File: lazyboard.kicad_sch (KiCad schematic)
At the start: 15 parts, among them J1 QWIIC/STEMMA, J2 Conn_01x06_Pin, J3 Conn_01x06_Pin, J4 Conn_01x03_Pin, J5 Conn_01x06_Pin, J6 Conn_01x06_Pin, P1 USB_C_Plug_USB2.0, SW1 SW_Push, SW2 SW_Push, U2 AP2112K-3.3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

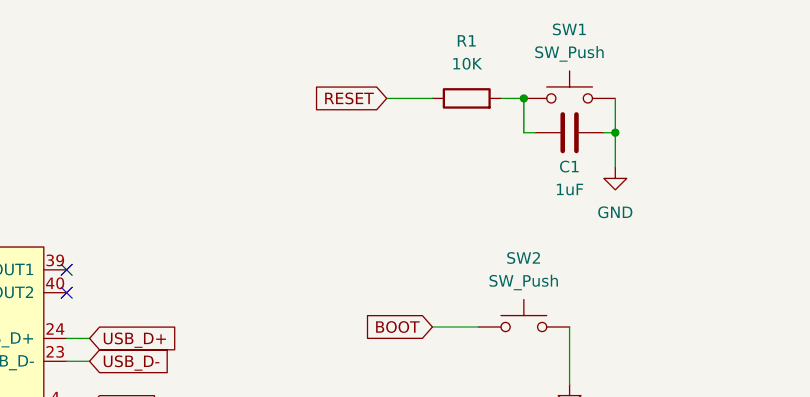
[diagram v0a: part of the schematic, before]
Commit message: fixed reset bug
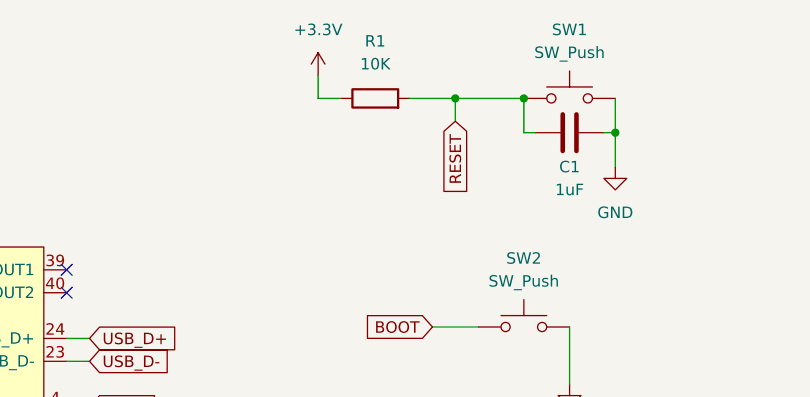
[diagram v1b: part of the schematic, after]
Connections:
- net +3.3V: now also R1.1
- net RESET: now also C1.1, R1.2, SW1.1; no longer R1.1
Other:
- moved on the sheet: R1
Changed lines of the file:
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@@
   (junction (at 85.09 124.46) (diameter 0) (color 0 0 0 0)
+  )
+  (junction (at 173.99 26.67) (diameter 0) (color 0 0 0 0)
   )
   (junction (at 53.34 156.21) (diameter 0) (color 0 0 0 0)
@@
     (stroke (width 0) (type default))
   )
-  (wire (pts (xy 179.07 26.67) (xy 181.61 26.67))
+  (wire (pts (xy 168.91 26.67) (xy 173.99 26.67))
     (stroke (width 0) (type default))
   )
@@
     (stroke (width 0) (type default))
   )
+  (wire (pts (xy 158.75 26.67) (xy 161.29 26.67))
+    (stroke (width 0) (type default))
+  )
   (wire (pts (xy 130.81 73.66) (xy 133.35 73.66))
     (stroke (width 0) (type default))
@@
     (stroke (width 0) (type default))
   )
-  (wire (pts (xy 166.37 26.67) (xy 171.45 26.67))
+  (wire (pts (xy 173.99 26.67) (xy 181.61 26.67))
     (stroke (width 0) (type default))
   )
@@
     (stroke (width 0) (type default))
   )
+  (wire (pts (xy 173.99 26.67) (xy 173.99 29.21))
+    (stroke (width 0) (type default))
+  )
   (wire (pts (xy 171.45 52.07) (xy 176.53 52.07))
     (stroke (width 0) (type default))
@@
     (stroke (width 0) (type default))
   )
+  (wire (pts (xy 158.75 24.13) (xy 158.75 26.67))
+    (stroke (width 0) (type default))
+  )
   (wire (pts (xy 130.81 78.74) (xy 133.35 78.74))
     (stroke (width 0) (type default))
@@
     )
   )
-  (global_label "RESET" (shape input) (at 166.37 26.67 180) (fields_autoplaced)
-    (effects (font (size 1.27 1.27)) (justify right))
-    (property "Intersheetrefs" "${INTERSHEET_REFS}" (at 157.6397 26.67 0)
+  (global_label "RESET" (shape input) (at 173.99 29.21 270) (fields_autoplaced)
+    (effects (font (size 1.27 1.27)) (justify right))
+    (property "Intersheetrefs" "${INTERSHEET_REFS}" (at 173.99 37.9403 90)
       (effects (font (size 1.27 1.27)) (justify right) hide)
     )
@@
     )
   )
-  (symbol (lib_id "Device:R") (at 175.26 26.67 90) (unit 1)
+  (symbol (lib_id "Device:R") (at 165.1 26.67 90) (unit 1)
     (in_bom yes) (on_board yes) (dnp no) (fields_autoplaced)
-    (property "Reference" "R1" (at 175.26 20.32 90)
+    (property "Reference" "R1" (at 165.1 20.32 90)
       (effects (font (size 1.27 1.27)))
     )
-    (property "Value" "10K" (at 175.26 22.86 90)
+    (property "Value" "10K" (at 165.1 22.86 90)
       (effects (font (size 1.27 1.27)))
     )
-    (property "Footprint" "Resistor_SMD:R_0603_1608Metric" (at 175.26 28.448 90)
+    (property "Footprint" "Resistor_SMD:R_0603_1608Metric" (at 165.1 28.448 90)
       (effects (font (size 1.27 1.27)) hide)
     )
-    (property "Datasheet" "~" (at 175.26 26.67 0)
+    (property "Datasheet" "~" (at 165.1 26.67 0)
       (effects (font (size 1.27 1.27)) hide)
     )
@@
         )
       )
+    )
+  )
+  (symbol (lib_id "power:+3.3V") (at 158.75 24.13 0) (unit 1)
+    (in_bom yes) (on_board yes) (dnp no) (fields_autoplaced)
+    (property "Reference" "#PWR012" (at 158.75 27.94 0)
+      (effects (font (size 1.27 1.27)) hide)
+    )
+    (property "Value" "+3.3V" (at 158.75 19.05 0)
+      (effects (font (size 1.27 1.27)))
+    )
+    (property "Footprint" "" (at 158.75 24.13 0)
+      (effects (font (size 1.27 1.27)) hide)
+    )
+    (property "Datasheet" "" (at 158.75 24.13 0)
+      (effects (font (size 1.27 1.27)) hide)
+    )
+    (pin "1")
+    (instances
+      (project "lazyboard"
+        (path "/4efe3317-2f39-4159-870e-db1a057467fb"
+          (reference "#PWR012") (unit 1)
+        )
+      )
